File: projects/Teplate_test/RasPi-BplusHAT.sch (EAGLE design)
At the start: 1 part, among them K1 PIN20X2

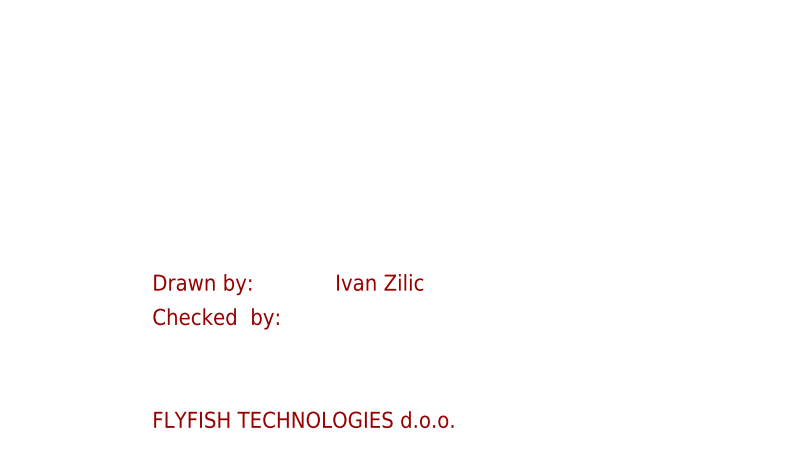
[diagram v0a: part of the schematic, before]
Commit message: Update RasPi-BplusHAT.sch
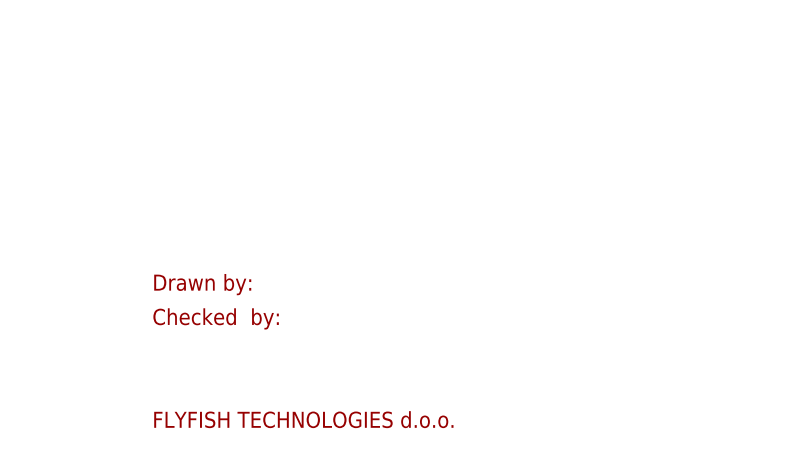
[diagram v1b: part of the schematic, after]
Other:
- note removed: "Ivan Zilic"
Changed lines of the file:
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@@
 <grid distance="0.1" unitdist="inch" unit="inch" style="lines" multiple="1" display="no" altdistance="0.01" altunitdist="inch" altunit="inch"/>
 <layers>
-<layer number="1" name="Top" color="4" fill="1" visible="no" active="no"/>
-<layer number="2" name="Route2" color="1" fill="3" visible="no" active="no"/>
-<layer number="3" name="Route3" color="4" fill="3" visible="no" active="no"/>
-<layer number="14" name="Route14" color="1" fill="6" visible="no" active="no"/>
-<layer number="15" name="Route15" color="4" fill="6" visible="no" active="no"/>
-<layer number="16" name="Bottom" color="1" fill="1" visible="no" active="no"/>
-<layer number="17" name="Pads" color="2" fill="1" visible="no" active="no"/>
-<layer number="18" name="Vias" color="2" fill="1" visible="no" active="no"/>
-<layer number="19" name="Unrouted" color="6" fill="1" visible="no" active="no"/>
-<layer number="20" name="Dimension" color="15" fill="1" visible="no" active="no"/>
-<layer number="21" name="tPlace" color="7" fill="1" visible="no" active="no"/>
-<layer number="22" name="bPlace" color="7" fill="1" visible="no" active="no"/>
-<layer number="23" name="tOrigins" color="15" fill="1" visible="no" active="no"/>
-<layer number="24" name="bOrigins" color="15" fill="1" visible="no" active="no"/>
-<layer number="25" name="tNames" color="7" fill="1" visible="no" active="no"/>
-<layer number="26" name="bNames" color="7" fill="1" visible="no" active="no"/>
-<layer number="27" name="tValues" color="7" fill="1" visible="no" active="no"/>
-<layer number="28" name="bValues" color="7" fill="1" visible="no" active="no"/>
+<layer number="1" name="Top" color="4" fill="1" visible="yes" active="no"/>
+<layer number="2" name="Route2" color="1" fill="3" visible="yes" active="no"/>
+<layer number="3" name="Route3" color="4" fill="3" visible="yes" active="no"/>
+<layer number="14" name="Route14" color="1" fill="6" visible="yes" active="no"/>
+<layer number="15" name="Route15" color="4" fill="6" visible="yes" active="no"/>
+<layer number="16" name="Bottom" color="1" fill="1" visible="yes" active="no"/>
+<layer number="17" name="Pads" color="2" fill="1" visible="yes" active="no"/>
+<layer number="18" name="Vias" color="2" fill="1" visible="yes" active="no"/>
+<layer number="19" name="Unrouted" color="6" fill="1" visible="yes" active="no"/>
+<layer number="20" name="Dimension" color="15" fill="1" visible="yes" active="no"/>
+<layer number="21" name="tPlace" color="7" fill="1" visible="yes" active="no"/>
+<layer number="22" name="bPlace" color="7" fill="1" visible="yes" active="no"/>
+<layer number="23" name="tOrigins" color="15" fill="1" visible="yes" active="no"/>
+<layer number="24" name="bOrigins" color="15" fill="1" visible="yes" active="no"/>
+<layer number="25" name="tNames" color="7" fill="1" visible="yes" active="no"/>
+<layer number="26" name="bNames" color="7" fill="1" visible="yes" active="no"/>
+<layer number="27" name="tValues" color="7" fill="1" visible="yes" active="no"/>
+<layer number="28" name="bValues" color="7" fill="1" visible="yes" active="no"/>
 <layer number="29" name="tStop" color="7" fill="3" visible="no" active="no"/>
 <layer number="30" name="bStop" color="7" fill="6" visible="no" active="no"/>
@@
 <layer number="35" name="tGlue" color="7" fill="4" visible="no" active="no"/>
 <layer number="36" name="bGlue" color="7" fill="5" visible="no" active="no"/>
-<layer number="37" name="tTest" color="7" fill="1" visible="no" active="no"/>
-<layer number="38" name="bTest" color="7" fill="1" visible="no" active="no"/>
+<layer number="37" name="tTest" color="7" fill="1" visible="yes" active="no"/>
+<layer number="38" name="bTest" color="7" fill="1" visible="yes" active="no"/>
 <layer number="39" name="tKeepout" color="4" fill="11" visible="no" active="no"/>
 <layer number="40" name="bKeepout" color="1" fill="11" visible="no" active="no"/>
@@
 <layer number="44" name="Drills" color="7" fill="1" visible="no" active="no"/>
 <layer number="45" name="Holes" color="7" fill="1" visible="no" active="no"/>
-<layer number="46" name="Milling" color="3" fill="1" visible="no" active="no"/>
-<layer number="47" name="Measures" color="7" fill="1" visible="no" active="no"/>
-<layer number="48" name="Document" color="7" fill="1" visible="no" active="no"/>
-<layer number="49" name="Reference" color="7" fill="1" visible="no" active="no"/>
-<layer number="50" name="dxf" color="7" fill="1" visible="no" active="no"/>
-<layer number="51" name="tDocu" color="7" fill="1" visible="no" active="no"/>
-<layer number="52" name="bDocu" color="7" fill="1" visible="no" active="no"/>
-<layer number="53" name="tGND_GNDA" color="7" fill="1" visible="no" active="no"/>
-<layer number="54" name="bGND_GNDA" color="7" fill="1" visible="no" active="no"/>
-<layer number="56" name="wert" color="7" fill="1" visible="no" active="no"/>
+<layer number="46" name="Milling" color="3" fill="1" visible="yes" active="no"/>
+<layer number="47" name="Measures" color="7" fill="1" visible="yes" active="no"/>
+<layer number="48" name="Document" color="7" fill="1" visible="yes" active="no"/>
+<layer number="49" name="Reference" color="7" fill="1" visible="yes" active="no"/>
+<layer number="50" name="dxf" color="7" fill="1" visible="yes" active="no"/>
+<layer number="51" name="tDocu" color="7" fill="1" visible="yes" active="no"/>
+<layer number="52" name="bDocu" color="7" fill="1" visible="yes" active="no"/>
+<layer number="53" name="tGND_GNDA" color="7" fill="1" visible="yes" active="no"/>
+<layer number="54" name="bGND_GNDA" color="7" fill="1" visible="yes" active="no"/>
+<layer number="56" name="wert" color="7" fill="1" visible="yes" active="no"/>
 <layer number="91" name="Nets" color="2" fill="1" visible="yes" active="yes"/>
 <layer number="92" name="Busses" color="1" fill="1" visible="yes" active="yes"/>
@@
 <text x="289.56" y="16.51" size="1.778" layer="94" ratio="15">Checked  by:</text>
 <text x="289.56" y="5.08" size="1.778" layer="94">FLYFISH TECHNOLOGIES d.o.o.</text>
-<text x="309.88" y="20.32" size="1.778" layer="94">Ivan Zilic</text>
 <text x="374.65" y="5.08" size="2.54" layer="94" ratio="10">v0.1</text>
 </plain>
